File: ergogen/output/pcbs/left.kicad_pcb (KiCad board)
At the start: 2 copper layers, 140.9 x 96.1 mm, 88 parts

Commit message: wip: v2
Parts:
- removed LED1, LED10, LED11, LED12, LED13, LED14, LED15, LED16, LED17, LED18, LED19, LED2, LED20, LED21, LED22, LED23, LED3, LED4, LED5, LED6, LED7, LED8, LED9: , ceoloide:led_SK6812mini-e (per-keysingle-side)
- removed LED24, LED25, LED26, LED27, LED28, LED29: VAL**, WS2812B
- G: moved to B.Cu
- moved G 123.2 mm to (156.2, 173.4), turned to 0 degrees
- moved S23 8.00 mm to (279.7, 187.1)
- moved D23 8.00 mm to (272.7, 182.6)
- moved S22 8.00 mm to (261.5, 179.6)
- moved D20 8.00 mm to (215.7, 176.6)
- moved D21 8.00 mm to (233.7, 176.6)
- moved S20 8.00 mm to (224.0, 177.0)
- moved S21 8.00 mm to (242.0, 177.0)
- moved D22 8.00 mm to (253.6, 177.0)
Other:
- board size 140.9 x 96.1 mm -> 129.3 x 92.4 mm
- net class Default added: clearance 0.2, trace_width 0.25, via_dia 0.8, via_drill 0.4

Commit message: wip: unrouted v2
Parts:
- removed H3, H4, H5, H6, H7: , ceoloide:mounting_hole_plated
- added MH1: , ceoloide:mounting_hole_npth, F.Cu at (251.0, 133.5)
- added MH2: , ceoloide:mounting_hole_npth, F.Cu at (179.0, 141.0)
- added MH3: , ceoloide:mounting_hole_npth, F.Cu at (179.0, 163.0)
- added MH4: , ceoloide:mounting_hole_npth, F.Cu at (251.0, 169.5)
- added MH5: , ceoloide:mounting_hole_npth, F.Cu at (272.6, 179.9)
- moved G 123.3 mm to (278.8, 160.3)
- moved H2 103.1 mm to (285.8, 178.3)
- moved D23 96.3 mm to (198.6, 121.2), turned to -90 degrees
- moved D19 66.2 mm to (215.7, 178.1)
- moved H1 59.1 mm to (271.8, 172.3)
- moved D13 48.0 mm to (233.7, 158.1)
- moved D16 45.2 mm to (251.7, 160.1)
- moved D10 39.8 mm to (215.7, 153.1)
- moved D22 20.4 mm to (272.7, 184.1), turned to -120 degrees
- moved D21 20.0 mm to (253.6, 178.5), turned to -105 degrees
- moved D20 18.1 mm to (233.7, 178.1)
- moved D17 16.5 mm to (251.7, 142.1)
- moved D18 16.5 mm to (251.7, 124.1)
- moved D11 14.5 mm to (215.7, 135.1)
- moved D12 14.5 mm to (215.7, 117.1)
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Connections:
- D10 pad 1: P017 -> P022
- D10 pad 2: ring_top -> middle_bottom
- D11 pad 1: P022 -> P020
- D11 pad 2: middle_bottom -> middle_home
- D12 pad 1: P020 -> P017
- D12 pad 2: middle_home -> middle_top
- D13 pad 1: P017 -> P022
- D13 pad 2: middle_top -> index_bottom
- D14 pad 1: P022 -> P020
- D14 pad 2: index_bottom -> index_home
- D15 pad 1: P020 -> P017
- D15 pad 2: index_home -> index_top
- D16 pad 1: P017 -> P022
- D16 pad 2: index_top -> inner_bottom
- D17 pad 1: P022 -> P020
- D17 pad 2: inner_bottom -> inner_home
- D18 pad 1: P020 -> P017
- D18 pad 2: inner_home -> inner_top
- D19 pad 1: P017 -> P024
- D19 pad 2: inner_top -> inner_thumb
- D20 pad 2: inner_thumb -> close_thumb
- D21 pad 2: close_thumb -> home_thumb
- D22 pad 2: home_thumb -> outer_thumb
- D23 pad 1: P024 -> P017
- D23 pad 2: outer_thumb -> ring_top
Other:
- board size 129.3 x 92.4 mm -> 130.6 x 90.5 mm

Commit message: wip: right routed
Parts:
- moved MH2 4.00 mm to (179.0, 145.0)
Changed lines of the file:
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@@
   (footprint "ceoloide:mounting_hole_npth"
     (layer "F.Cu")
-    (at 179 141 0)
+    (at 179 145 0)
     (property "Reference" "MH2"
       (at 0 2.55 0)

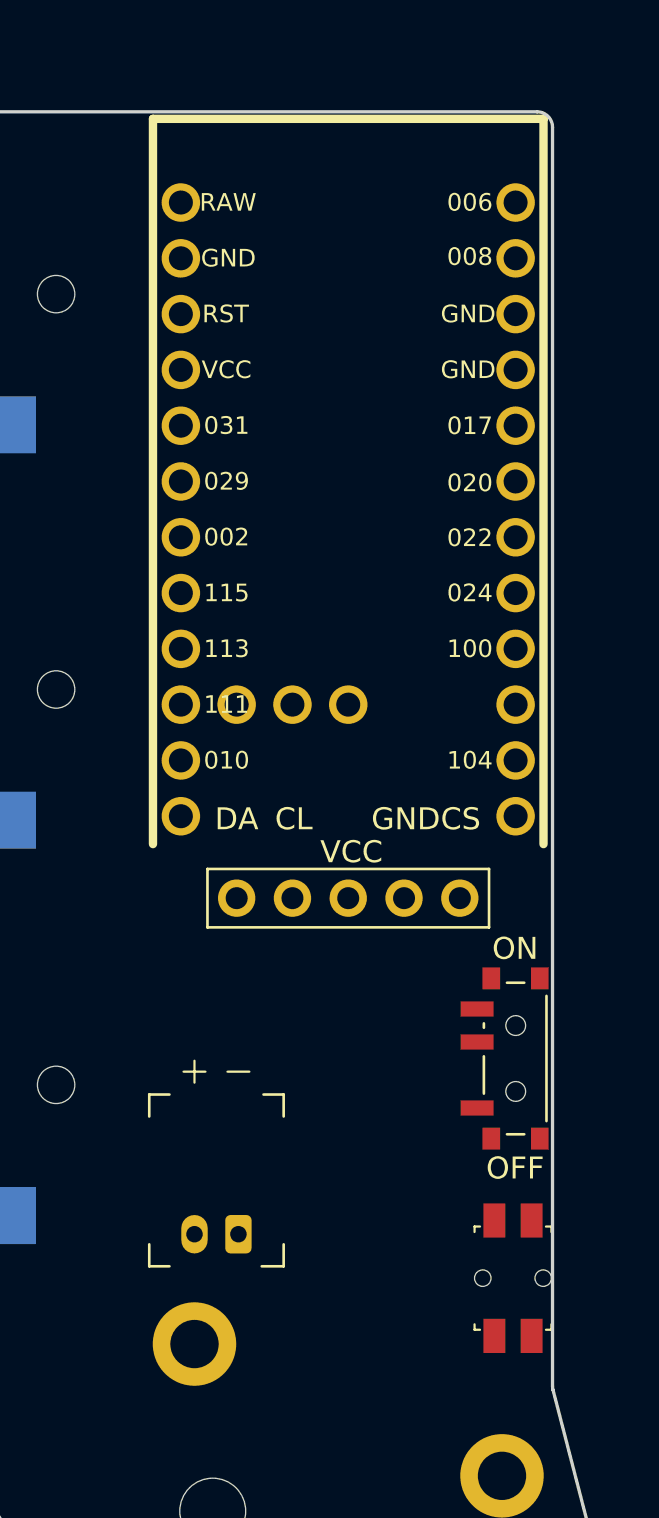
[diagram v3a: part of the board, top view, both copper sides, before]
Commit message: wip: change nice view pins / reroute
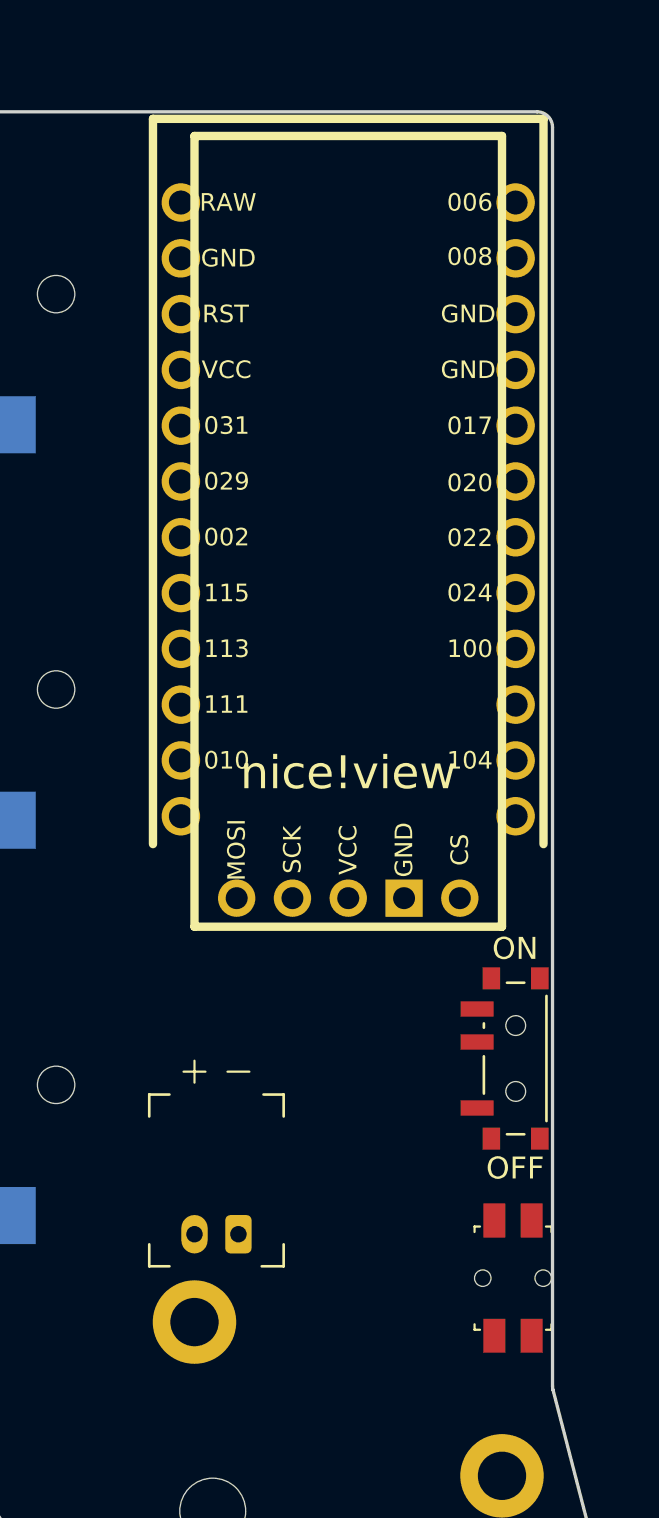
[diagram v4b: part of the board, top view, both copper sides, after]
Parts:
- removed DISP1: , ceoloide:display_nice_view
- added niceView1: niceView, lib:niceView_headers, F.Cu at (278.8, 153.3)
- moved H1 1.00 mm to (271.8, 171.3)
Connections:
- D1 pad 1: P022 -> P011
- D10 pad 1: P022 -> P011
- D11 pad 1: P020 -> P100
- D12 pad 1: P017 -> P024
- D13 pad 1: P022 -> P011
- D14 pad 1: P020 -> P100
- D15 pad 1: P017 -> P024
- D16 pad 1: P022 -> P011
- D17 pad 1: P020 -> P100
- D18 pad 1: P017 -> P024
- D19 pad 1: P024 -> P104
- D2 pad 1: P020 -> P100
- D20 pad 1: P024 -> P104
- D21 pad 1: P024 -> P104
- D22 pad 1: P024 -> P104
- D23 pad 1: P017 -> P024
- D3 pad 1: P017 -> P024
- D4 pad 1: P022 -> P011
- D5 pad 1: P020 -> P100
- D6 pad 1: P017 -> P024
- D7 pad 1: P024 -> P104
- D8 pad 1: P022 -> P011
- D9 pad 1: P020 -> P100

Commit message: add: v2 gerbers
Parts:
- moved RST1 0.10 mm to (286.2, 169.3)
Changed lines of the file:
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@@
   (footprint "ceoloide:reset_switch_smd_side"
     (layer "F.Cu")
-    (at 286.3 169.3 -90)
+    (at 286.2 169.3 -90)
     (property "Reference" "RST1"
       (at 0 0 -90)
